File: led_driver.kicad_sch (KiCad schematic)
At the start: 10 parts, among them J2 Conn_01x10_Pin, J3 Conn_01x10_Pin, U4 STP16CP05XT

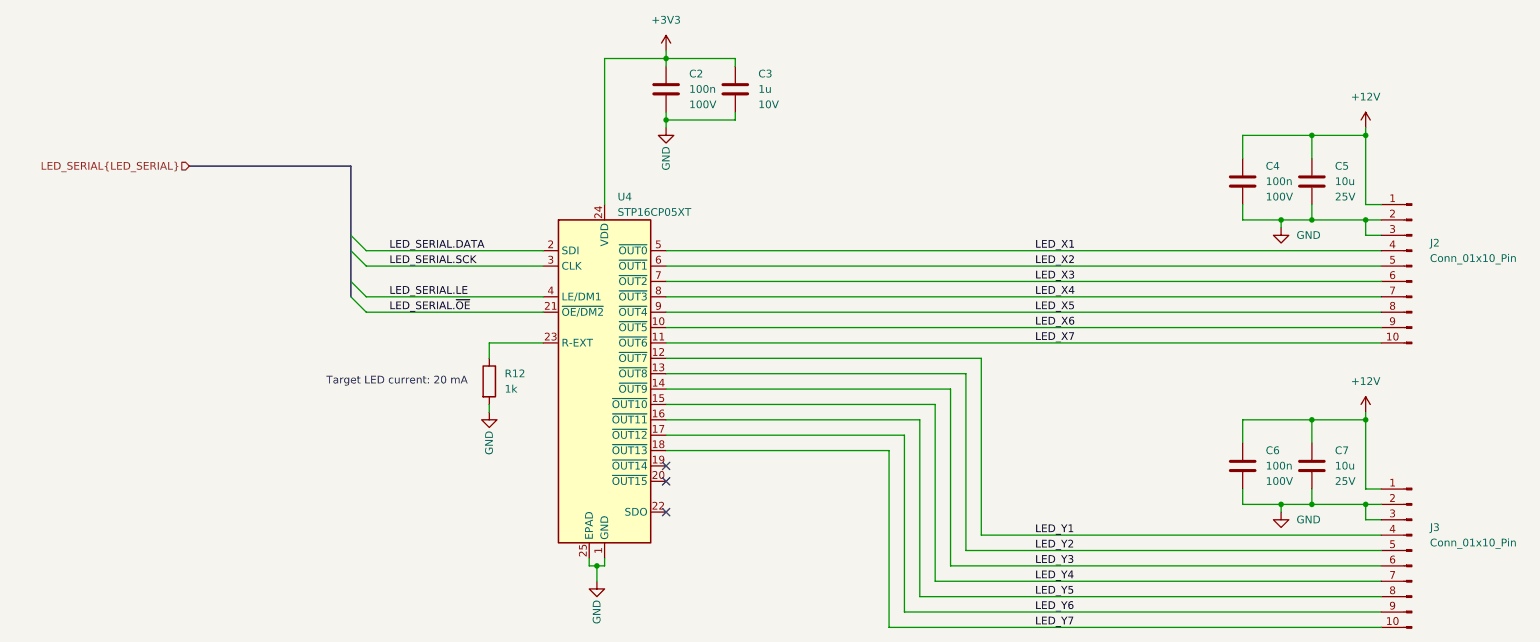
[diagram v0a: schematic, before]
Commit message: nodified according to review
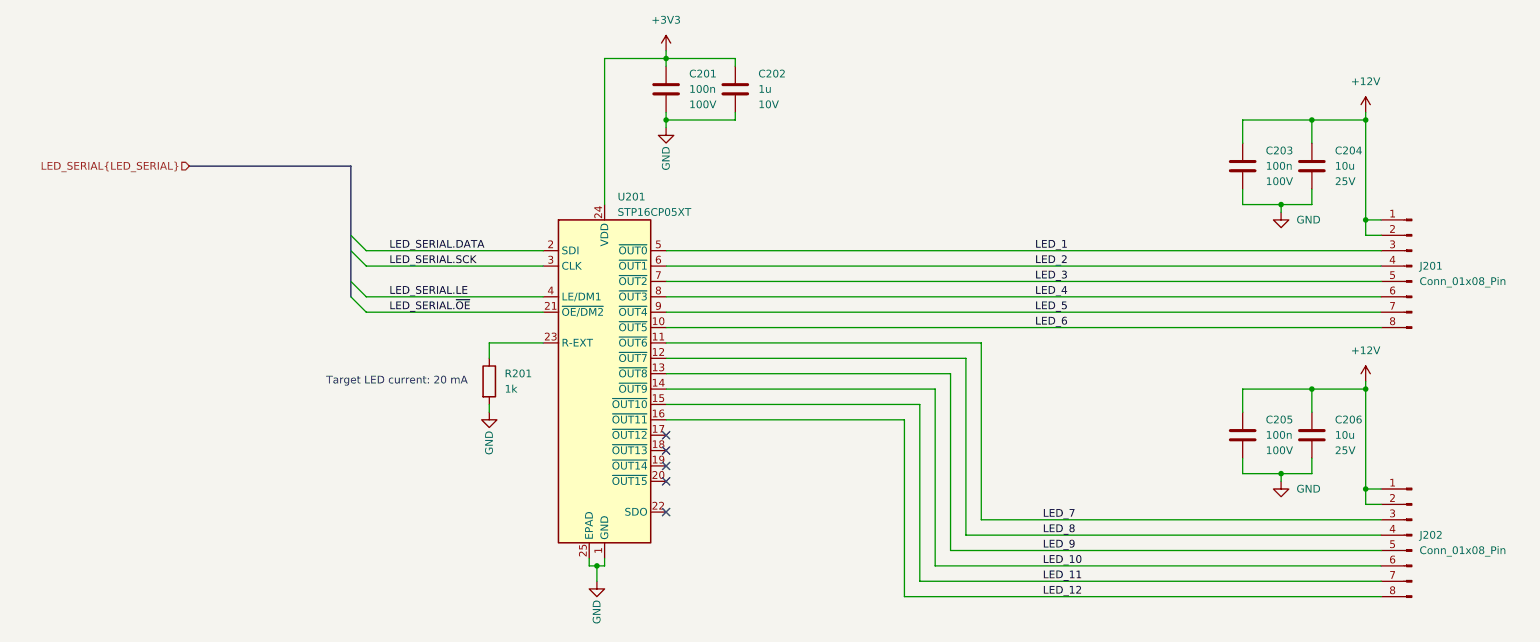
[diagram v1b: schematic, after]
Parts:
- removed C6: 100n, symbol Capacitor_Protonica:C_voltage
- removed C7: 10u, symbol Capacitor_Protonica:C_voltage
- removed J2, J3: Conn_01x10_Pin, symbol Connector:Conn_01x10_Pin
- added C205: 100n, symbol Capacitor_Protonica:C_voltage
- added C206: 10u, symbol Capacitor_Protonica:C_voltage
- added J201, J202: Conn_01x08_Pin, symbol Connector:Conn_01x08_Pin
- renumbered C2 to C201, C3 to C202, C4 to C203, C5 to C204, R12 to R201, U4 to U201
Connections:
- net +12V: now also C205.1, C206.1, J201.1 (Pin_1), J201.2 (Pin_2), J202.1 (Pin_1), J202.2 (Pin_2)
- net GND: now also C205.2, C206.2
- net LED_X1 renamed LED_1
- net LED_1: now also J201.3 (Pin_3)
- net LED_X2 renamed LED_2
- net LED_2: now also J201.4 (Pin_4)
- net LED_X3 renamed LED_3
- net LED_3: now also J201.5 (Pin_5)
- net LED_X4 renamed LED_4
- net LED_4: now also J201.6 (Pin_6)
- net LED_X5 renamed LED_5
- net LED_5: now also J201.7 (Pin_7)
- net LED_X6 renamed LED_6
- net LED_6: now also J201.8 (Pin_8)
- net LED_X7 renamed LED_7
- net LED_7: now also J202.3 (Pin_3)
- net LED_Y1 renamed LED_8
- net LED_8: now also J202.4 (Pin_4)
- net LED_Y2 renamed LED_9
- net LED_9: now also J202.5 (Pin_5)
- net LED_Y3 renamed LED_10
- net LED_10: now also J202.6 (Pin_6)
- net LED_Y4 renamed LED_11
- net LED_11: now also J202.7 (Pin_7)
- net LED_Y5 renamed LED_12
- net LED_12: now also J202.8 (Pin_8)
- net LED_Y6: no longer names the net of U201.17 (~{OUT12})
- net LED_Y7: no longer names the net of U201.18 (~{OUT13})
- no-connect marks 3 -> 5
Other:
- title: LED Interface -> Front End Electronics
- moved on the sheet: C203, C204

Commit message: footprints associated to symbols
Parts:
- C201, C203, C205: footprint (none) -> Capacitor_SMD:C_0805_2012Metric_Pad1.18x1.45mm_HandSolder; MPN (none) -> GCM21BR72A104KA37L; Manufacturer (none) -> Murata Electronics
- C202: footprint (none) -> Capacitor_SMD:C_0805_2012Metric_Pad1.18x1.45mm_HandSolder; MPN (none) -> GRM21BR71A105KA01L; Manufacturer (none) -> Murata Electronics
- C204, C206: footprint (none) -> Capacitor_SMD:C_1206_3216Metric_Pad1.33x1.80mm_HandSolder; MPN (none) -> GRM31CR71E106KA12L; Manufacturer (none) -> Murata Electronics
- J201, J202: footprint (none) -> Connector_PinHeader_2.54mm:PinHeader_1x08_P2.54mm_Vertical
- R201: footprint (none) -> Resistor_SMD:R_0805_2012Metric_Pad1.20x1.40mm_HandSolder; MPN (none) -> CRCW08051K00FKEA; Manufacturer (none) -> Vishay Dale
- U201: MPN (none) -> STP16CP05XTTR; Manufacturer (none) -> STMicroelectronics

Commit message: Most tracks routed
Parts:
- J201, J202: footprint Connector_PinHeader_2.54mm:PinHeader_1x08_P2.54mm_Vertical -> Connector_PinHeader_2.54mm:PinHeader_2x04_P2.54mm_Vertical
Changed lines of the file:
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@@
 			)
 		)
-		(property "Footprint" "Connector_PinHeader_2.54mm:PinHeader_1x08_P2.54mm_Vertical"
+		(property "Footprint" "Connector_PinHeader_2.54mm:PinHeader_2x04_P2.54mm_Vertical"
 			(at 353.06 102.87 0)
 			(hide yes)
@@
 			)
 		)
-		(property "Footprint" "Connector_PinHeader_2.54mm:PinHeader_1x08_P2.54mm_Vertical"
+		(property "Footprint" "Connector_PinHeader_2.54mm:PinHeader_2x04_P2.54mm_Vertical"
 			(at 353.06 147.32 0)
 			(hide yes)

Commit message: minor changes
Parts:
- J201, J202: value Conn_01x08_Pin -> Conn_02x04_Pin; MPN (none) -> PR20204VBDN; Manufacturer (none) -> METZ CONNECT
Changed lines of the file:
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@@
 			)
 		)
-		(property "Description" ""
+		(property "Description" "CAP CER 1UF 10V X7R 0805"
 			(at 230.886 62.23 0)
 			(hide yes)
@@
 			)
 		)
-		(property "Value" "Conn_01x08_Pin"
+		(property "Value" "Conn_02x04_Pin"
 			(at 354.33 105.4099 0)
 			(show_name no)
@@
 			)
 		)
-		(property "Description" "CONN HEADER R/A 8POS 2.54MM"
+		(property "Description" "CONN HEADER VERTICAL 8POS 2.54MM"
 			(at 353.06 102.87 0)
 			(hide yes)
@@
 			)
 		)
-		(property "MPN" ""
+		(property "MPN" "PR20204VBDN"
 			(at 353.06 102.87 0)
 			(hide yes)
@@
 			)
 		)
-		(property "Manufacturer" ""
+		(property "Manufacturer" "METZ CONNECT"
 			(at 353.06 102.87 0)
 			(hide yes)
@@
 			)
 		)
-		(property "Value" "Conn_01x08_Pin"
+		(property "Value" "Conn_02x04_Pin"
 			(at 354.33 149.8599 0)
 			(show_name no)
@@
 			)
 		)
-		(property "Description" "CONN HEADER R/A 8POS 2.54MM"
+		(property "Description" "CONN HEADER VERTICAL 8POS 2.54MM"
 			(at 353.06 147.32 0)
 			(hide yes)
@@
 			)
 		)
-		(property "MPN" ""
+		(property "MPN" "PR20204VBDN"
 			(at 353.06 147.32 0)
 			(hide yes)
@@
 			)
 		)
-		(property "Manufacturer" ""
+		(property "Manufacturer" "METZ CONNECT"
 			(at 353.06 147.32 0)
 			(hide yes)

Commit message: updated bom, ready for ordering
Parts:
- J201, J202: MPN PR20204VBDN -> M20-9760442; Manufacturer METZ CONNECT -> Harwin Inc.
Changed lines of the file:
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@@
 			)
 		)
-		(property "Description" "CONN HEADER VERTICAL 8POS 2.54MM"
-			(at 353.06 102.87 0)
-			(hide yes)
-			(show_name no)
-			(do_not_autoplace no)
-			(effects
-				(font
-					(size 1.27 1.27)
-				)
-			)
-		)
-		(property "MPN" "PR20204VBDN"
-			(at 353.06 102.87 0)
-			(hide yes)
-			(show_name no)
-			(do_not_autoplace no)
-			(effects
-				(font
-					(size 1.27 1.27)
-				)
-			)
-		)
-		(property "Manufacturer" "METZ CONNECT"
+		(property "Description" "CONN HEADER VERT 8POS 2.54MM"
+			(at 353.06 102.87 0)
+			(hide yes)
+			(show_name no)
+			(do_not_autoplace no)
+			(effects
+				(font
+					(size 1.27 1.27)
+				)
+			)
+		)
+		(property "MPN" "M20-9760442"
+			(at 353.06 102.87 0)
+			(hide yes)
+			(show_name no)
+			(do_not_autoplace no)
+			(effects
+				(font
+					(size 1.27 1.27)
+				)
+			)
+		)
+		(property "Manufacturer" "Harwin Inc."
 			(at 353.06 102.87 0)
 			(hide yes)
@@
 			)
 		)
-		(property "Description" "CONN HEADER VERTICAL 8POS 2.54MM"
-			(at 353.06 147.32 0)
-			(hide yes)
-			(show_name no)
-			(do_not_autoplace no)
-			(effects
-				(font
-					(size 1.27 1.27)
-				)
-			)
-		)
-		(property "MPN" "PR20204VBDN"
-			(at 353.06 147.32 0)
-			(hide yes)
-			(show_name no)
-			(do_not_autoplace no)
-			(effects
-				(font
-					(size 1.27 1.27)
-				)
-			)
-		)
-		(property "Manufacturer" "METZ CONNECT"
-			(at 353.06 147.32 0)
-			(hide yes)
+		(property "Description" "CONN HEADER VERT 8POS 2.54MM"
+			(at 353.06 147.32 0)
+			(hide yes)
+			(show_name no)
+			(do_not_autoplace no)
+			(effects
+				(font
+					(size 1.27 1.27)
+				)
+			)
+		)
+		(property "MPN" "M20-9760442"
+			(at 353.06 147.32 0)
+			(hide yes)
+			(show_name no)
+			(do_not_autoplace no)
+			(effects
+				(font
+					(size 1.27 1.27)
+				)
+			)
+		)
+		(property "Manufacturer" "Harwin Inc."
+			(at 353.06 147.32 0)
+			(hide yes)
